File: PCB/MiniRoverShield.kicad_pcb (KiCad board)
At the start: 2 copper layers, 75 x 66.3 mm, 47 parts, among them J1 linetracer, J2 linetracer, J3 linetracer, J4 linetracer, J5 linetracer, J6 linetracer, P1 Arduino nano 33, P2 Arduino nano 33, P3 flightPin, P4 Nichrome, P5 Motor, P6 Motor, Q1 FDS4935A, Q2 IRFML8244TRPbF, Q3 L-51ROPT1D1, Q4 L-51ROPT1D1, SW1 Power, U1 TPS63000, U2 GYSFDMAXB, U3 BD6211F, U4 BD6211F

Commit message: 配線完了
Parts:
- moved R14 1.91 mm to (78.1, 74.1), turned to 0 degrees
- moved R13 1.46 mm to (78.0, 71.6), turned to 180 degrees
- turned U3 to 180 degrees
- turned U4 to 180 degrees
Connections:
- P1 pad 1: /CS -> /SCK
- P1 pad 11: Net-(P1-Pad11) -> /PTr_R
- P1 pad 5: /PTr_R -> /RTr_L
- P1 pad 6: /RTr_L -> Net-(P1-Pad6)
- P2 pad 10: Net-(P2-Pad10) -> /flightPin
- P2 pad 11: Net-(P2-Pad11) -> /CS
- P2 pad 12: /MotorR2 -> /MotorL2
- P2 pad 13: /MotorR1 -> /MotorL1
- P2 pad 5: /flightPin -> Net-(P2-Pad5)
- P2 pad 8: /MotorL2 -> /MotorR2
- P2 pad 9: /MotorL1 -> /MotorR1
- SD1 pad 5: /CLK -> /SCK
- U3 pad 1: Net-(P5-Pad1) -> Net-(P5-Pad2)
- U3 pad 7: Net-(P5-Pad2) -> Net-(P5-Pad1)
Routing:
- net +VSW: track 0.00 -> 239.9 mm, vias 0 -> 6
- net +3V3: track 0.00 -> 163.9 mm, vias 0 -> 3
- net +BATT: track 0.00 -> 88.8 mm, vias 0 -> 5
- net GND: track 0.00 -> 80.3 mm, vias 0 -> 121
- net /RTr_L: track 0.00 -> 58.0 mm
- net /SCK: track 0.00 -> 40.2 mm, vias 0 -> 1
- net /MotorR1: track 0.00 -> 39.8 mm, vias 0 -> 3
- net /Arduino→GPS: track 0.00 -> 36.1 mm, vias 0 -> 2
- net /MotorL1: track 0.00 -> 34.4 mm, vias 0 -> 1
- net /PTr_R: track 0.00 -> 33.8 mm, vias 0 -> 1
- net Net-(R2-Pad1): track 0.00 -> 32.6 mm, vias 0 -> 1
- net /flightPin: track 0.00 -> 32.4 mm, vias 0 -> 1
- net /Arduino←GPS: track 0.00 -> 31.7 mm
- net /MotorL2: track 0.00 -> 29.7 mm, vias 0 -> 1
- net Net-(D3-Pad2): track 0.00 -> 27.7 mm
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- added copper zone on B.Cu, net GND
- added copper zone on F.Cu, net GND
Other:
- net class 3.3V added: clearance 0.2, trace_width 0.8, via_dia 1, via_drill 0.5
- net class Default: clearance 0.2 -> 0.1524; trace_width 0.25 -> 0.2; via_dia 0.8 -> 0.6; via_drill 0.4 -> 0.3
- net class Vbat added: clearance 0.3, trace_width 1.5, via_dia 1.5, via_drill 0.8
- rule trace_clearance: 0.2 -> 0.1524
- rule trace_min: 0.2 -> 0.1524
- rule via_min_size: 0.4 -> 0.3
- board text added: "+"
- board text added: "-"
- board text added: "Li-ion 10440 3.7V"
- board text added: "ON OFF"

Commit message: Add Silk
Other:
- board text added: "2019.08.03 @n_yosihisa MiniRoverShield for Arduino nano 33"
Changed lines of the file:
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@@
   (general
     (thickness 1.6)
-    (drawings 88)
+    (drawings 89)
     (tracks 684)
     (zones 0)
@@
   )
   (setup
-    (last_trace_width 0.1524)
+    (last_trace_width 0.2)
     (user_trace_width 0.1524)
     (user_trace_width 0.2)
@@
     )
   )
+  (gr_text "2019.08.03\n@n_yosihisa\nMiniRoverShield for Arduino nano 33" (at 41.82 94.666) (layer F.SilkS)
+    (effects (font (size 1.2 1.2) (thickness 0.2)) (justify left))
+  )
   (gr_poly (pts (xy 92.112 82.982) (xy 92.112 78.664) (xy 94.398 78.664) (xy 94.398 82.982)) (layer F.SilkS) (width 0.15))

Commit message: Add Gerber
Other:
- board text added: "2019.08.03 @n_yosihisa MiniRoverShield for Arduino nano 33 Ver0.1"
- board text removed: "2019.08.03 @n_yosihisa MiniRoverShield for Arduino nano 33"
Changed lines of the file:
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@@
   (general
     (thickness 1.6)
-    (drawings 89)
+    (drawings 90)
     (tracks 684)
     (zones 0)
@@
     (pad_drill 0.762)
     (pad_to_mask_clearance 0)
-    (aux_axis_origin 0 0)
+    (aux_axis_origin 40.55 46.93)
     (grid_origin 40.55 47.93)
     (visible_elements 7FFFFFFF)
     (pcbplotparams
-      (layerselection 0x010fc_ffffffff)
-      (usegerberextensions false)
+      (layerselection 0x010f0_ffffffff)
+      (usegerberextensions true)
       (usegerberattributes false)
       (usegerberadvancedattributes false)
@@
       (plotinvisibletext false)
       (padsonsilk false)
-      (subtractmaskfromsilk false)
+      (subtractmaskfromsilk true)
       (outputformat 1)
       (mirror false)
-      (drillshape 1)
+      (drillshape 0)
       (scaleselection 1)
-      (outputdirectory ""))
+      (outputdirectory "Gerber/"))
   )
   (net 0 "")
@@
     )
   )
-  (gr_text "2019.08.03\n@n_yosihisa\nMiniRoverShield for Arduino nano 33" (at 41.82 94.666) (layer F.SilkS)
+  (target plus (at 40.55 46.93) (size 1) (width 0.1) (layer Edge.Cuts))
+  (gr_text "2019.08.03\n@n_yosihisa\nMiniRoverShield for Arduino nano 33 Ver0.1" (at 41.82 94.666) (layer F.SilkS)
     (effects (font (size 1.2 1.2) (thickness 0.2)) (justify left))
   )

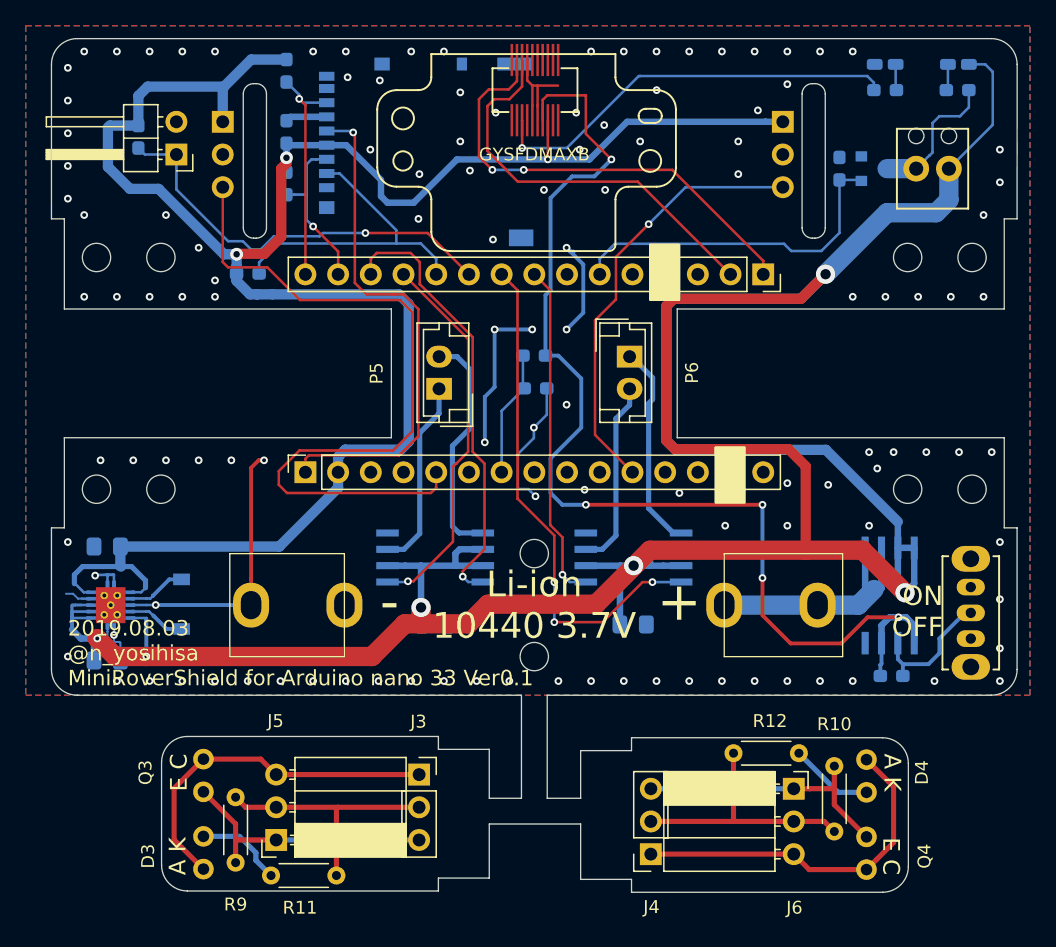
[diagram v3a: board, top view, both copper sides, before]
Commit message: Remove Line Trace
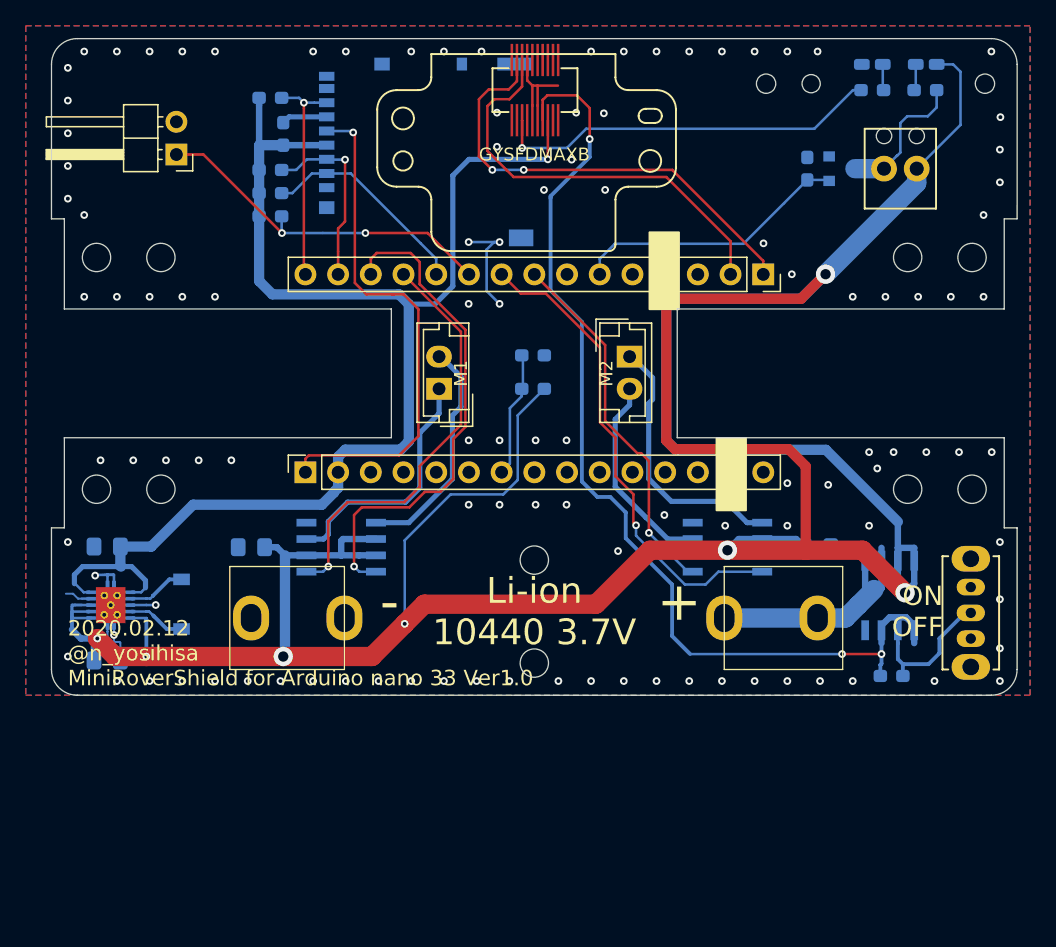
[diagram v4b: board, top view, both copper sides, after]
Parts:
- removed D3, D4: OSI5LA5A33A-B, user:LED_5mm_2.54mm
- removed the J1 at (97.3, 53.4)
- removed J2: linetracer, Connector_PinHeader_2.54mm:PinHeader_1x03_P2.54mm_Vertical
- removed J3, J4: linetracer, Connector_PinSocket_2.54mm:PinSocket_1x03_P2.54mm_Vertical
- removed J5, J6: linetracer, Connector_PinSocket_2.54mm:PinSocket_1x03_P2.54mm_Horizontal
- removed Q3, Q4: L-51ROPT1D1, user:LED_5mm_2.54mm
- removed R10, R11, R12, R9: 1K, Resistor_THT:R_Axial_DIN0204_L3.6mm_D1.6mm_P5.08mm_Horizontal
- Q1, U3, U4: footprint Package_SO:SO-8_5.3x6.2mm_P1.27mm -> Package_SO:SOIC-8_3.9x4.9mm_P1.27mm
- moved C5 15.5 mm to (100.0, 86.4)
- moved C4 15.5 mm to (56.1, 86.4), turned to 180 degrees
- moved R8 12.0 mm to (57.5, 60.7), turned to 0 degrees
- moved U3 7.34 mm to (63.0, 86.4)
- moved U4 7.34 mm to (93.0, 86.4)
- moved R7 6.49 mm to (57.5, 58.9)
- moved R13 2.58 mm to (78.0, 74.1)
- moved R14 2.57 mm to (78.0, 71.5)
- moved D2 2.50 mm to (108.5, 48.9)
- moved N1 2.50 mm to (109.2, 53.9)
- moved Q2 2.50 mm to (102.0, 57.0)
- moved R3 2.50 mm to (99.2, 57.0)
- moved R4 2.50 mm to (108.4, 50.9)
- moved R5 2.44 mm to (57.5, 51.5), turned to 0 degrees
- moved R6 1.63 mm to (57.5, 57.1), turned to 0 degrees
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- renumbered P3 to J1, P5 to M1, P6 to M2, P4 to N1, U2 to P3, R6 to R5, R7 to R6, R8 to R7, R5 to R8
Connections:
- P1 pad 11: /PTr_R -> Net-(P1-Pad11)
- P1 pad 5: /RTr_L -> Net-(P1-Pad5)
- R13 pad 1: +BATT -> +VSW
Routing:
- net /RTr_L: track 58.0 -> 0.00 mm
- net +3V3: track 163.9 -> 107.4 mm, vias 3 -> 1
- net GND: track 80.3 -> 39.1 mm, vias 121 -> 110
- net /PTr_R: track 33.8 -> 0.00 mm, vias 1 -> 0
- net Net-(D3-Pad2): track 27.7 -> 0.00 mm
- net Net-(D4-Pad2): track 27.5 -> 0.00 mm
- net +VSW: track 239.9 -> 265.5 mm, vias 6 -> 7
- net Net-(J3-Pad3): track 20.8 -> 0.00 mm
- net Net-(J4-Pad3): track 20.8 -> 0.00 mm
- net Net-(J4-Pad2): track 19.9 -> 0.00 mm
- net Net-(J3-Pad2): track 19.9 -> 0.00 mm
- net +BATT: track 88.8 -> 77.8 mm, vias 5 -> 3
- net /CS: track 25.2 -> 16.6 mm
- net Net-(D3-Pad1): track 6.86 -> 0.00 mm
- net Net-(D4-Pad1): track 6.52 -> 0.00 mm
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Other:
- board size 75 x 66.3 mm -> 75 x 51 mm
- board text added: "2020.02.12 @n_yosihisa MiniRoverShield for Arduino nano 33 Ver1.0"
- board text removed: "2019.08.03 @n_yosihisa MiniRoverShield for Arduino nano 33 Ver0.1"
- board text removed: "A K"
- board text removed: "E C"

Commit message: Change inductor
VLF4012AT-2R2をVLS3012HBX-2R2Mに変更
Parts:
- L1: footprint user:inductor_VLF4012-2R2 -> user_library:TDK_VLS3012
- moved L1 0.40 mm to (51.1, 90.9)
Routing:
- net GND: track 39.1 -> 50.2 mm, vias 110 -> 111
- net (no net): vias 1 -> 0
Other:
- outline, holes or cut-outs redrawn
- board text added: "2020.08.01 @n_yosihisa MiniRoverShield for Arduino nano 33 Ver1.1"
- board text removed: "2020.02.12 @n_yosihisa MiniRoverShield for Arduino nano 33 Ver1.0"

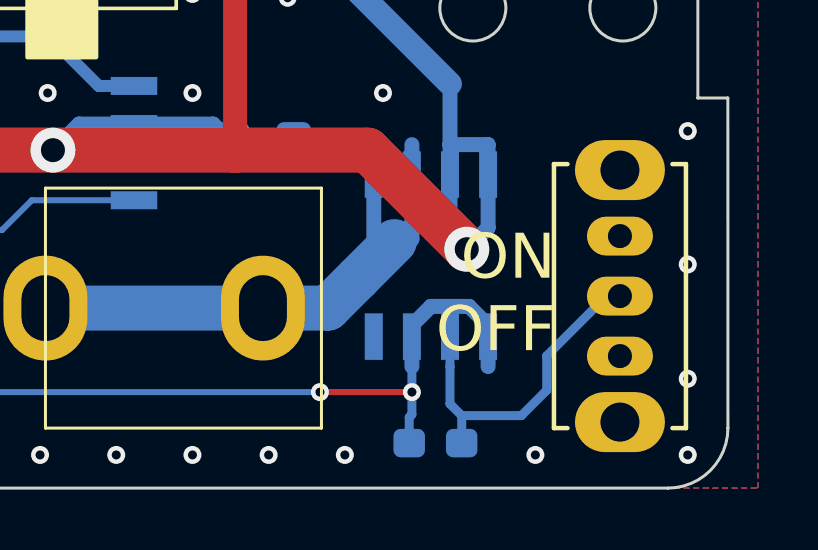
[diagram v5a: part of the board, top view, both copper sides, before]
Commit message: FET裏のパターン修正
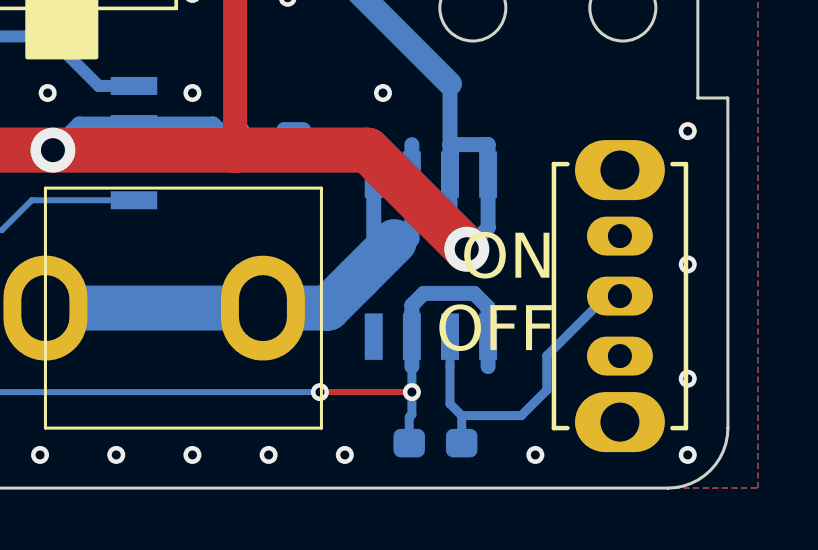
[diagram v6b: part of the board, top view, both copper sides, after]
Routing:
- net +BATT: track 77.8 -> 79.6 mm
